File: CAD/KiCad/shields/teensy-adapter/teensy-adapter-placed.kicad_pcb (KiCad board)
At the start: 2 copper layers, 53.3 x 101.6 mm, 73 parts, among them U1 SN74LV4T125PWR, U2 SN74LV4T125PWR, U3 SN74LV4T125PWR, U4 SN74LV4T125PWR

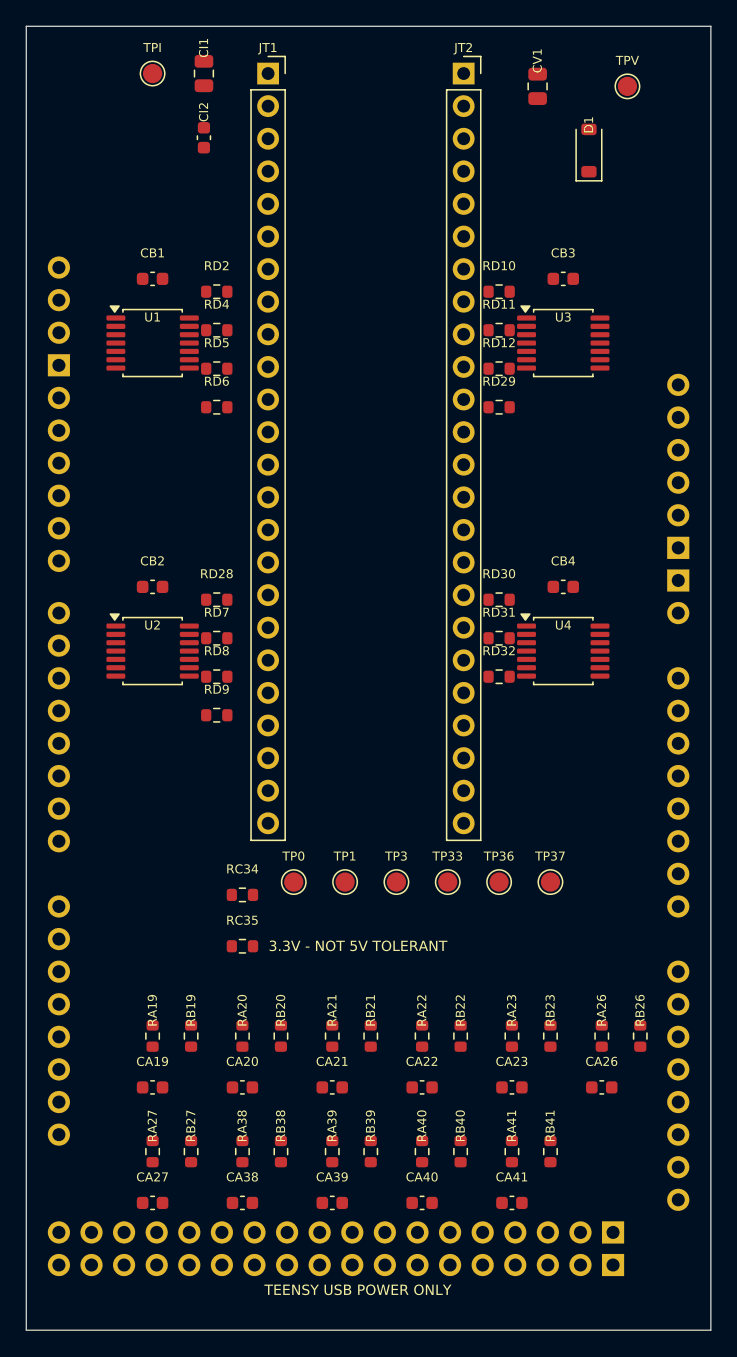
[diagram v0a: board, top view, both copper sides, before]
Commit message: Route the shield set and validate shared interfaces
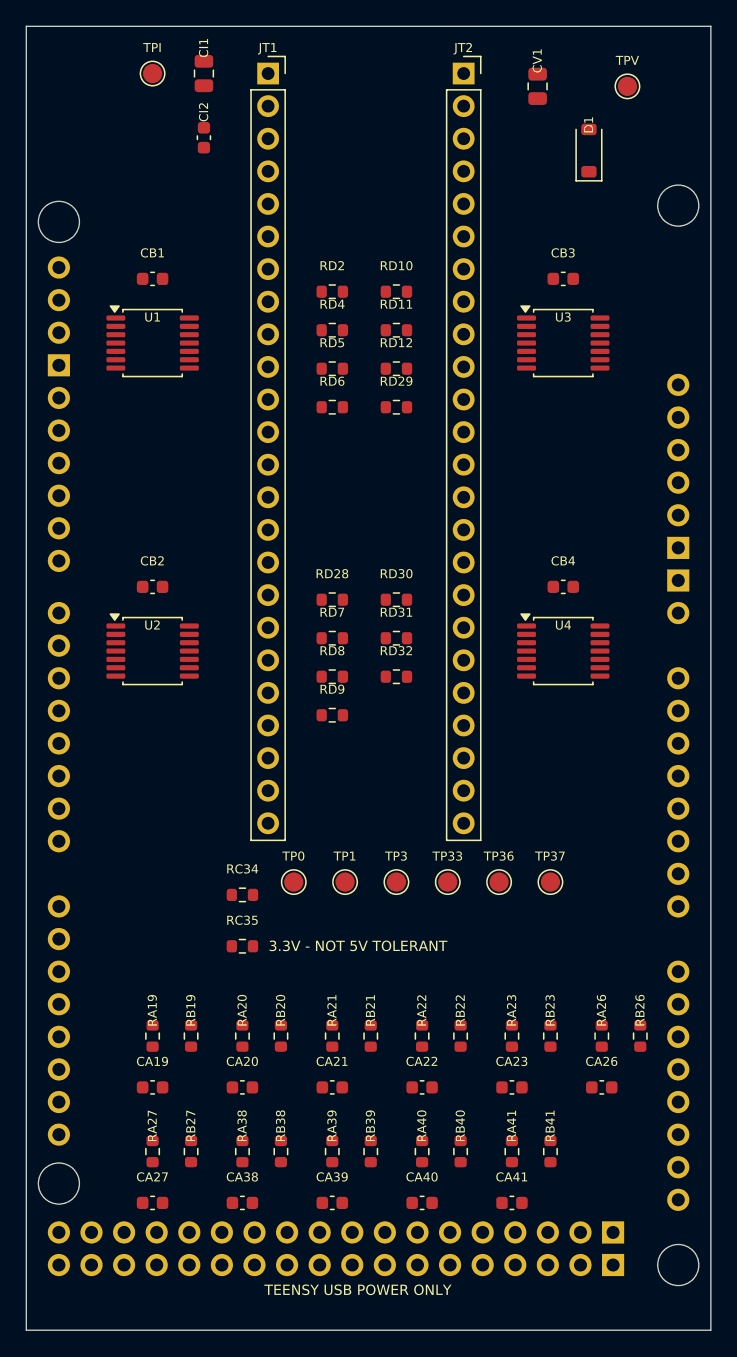
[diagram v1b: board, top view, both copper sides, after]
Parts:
- added HM1: M3 computing shield, Shields:MountingHole_3.2mm_M3, F.Cu at (192.0, 149.8)
- added HM2: M3 computing shield, Shields:MountingHole_3.2mm_M3, F.Cu at (143.7, 68.6)
- added HM3: M3 computing shield, Shields:MountingHole_3.2mm_M3, F.Cu at (143.7, 143.5)
- added HM4: M3 computing shield, Shields:MountingHole_3.2mm_M3, F.Cu at (192.0, 67.3)
- moved RD2 9.00 mm to (165.0, 74.0)
- moved RD28 9.00 mm to (165.0, 98.0)
- moved RD4 9.00 mm to (165.0, 77.0)
- moved RD5 9.00 mm to (165.0, 80.0)
- moved RD6 9.00 mm to (165.0, 83.0)
- moved RD7 9.00 mm to (165.0, 101.0)
- moved RD8 9.00 mm to (165.0, 104.0)
- moved RD9 9.00 mm to (165.0, 107.0)
- moved RD10 8.00 mm to (170.0, 74.0)
- moved RD11 8.00 mm to (170.0, 77.0)
- moved RD12 8.00 mm to (170.0, 80.0)
- moved RD29 8.00 mm to (170.0, 83.0)
- moved RD30 8.00 mm to (170.0, 98.0)
- moved RD31 8.00 mm to (170.0, 101.0)
- moved RD32 8.00 mm to (170.0, 104.0)

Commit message: Remove shield identification and adopt the simplified connector and Teensy pin maps
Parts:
- added TP40: gpio/40, Shields:TestPoint_Pad_D1.5mm, F.Cu at (186.0, 120.0)
- added TP41: gpio/41, Shields:TestPoint_Pad_D1.5mm, F.Cu at (190.0, 120.0)
- added TPG: GND, Shields:TestPoint_Pad_D1.5mm, F.Cu at (185.0, 124.0)
- D1: value SS14 -> 1N5819HW
- renumbered CA26 to CA24, CA27 to CA25, CA38 to CA26, CA39 to CA27, CA40 to CA38, CA41 to CA39, RA26 to RA24, RA27 to RA25, RA38 to RA26, RA39 to RA27, RA40 to RA38, RA41 to RA39, RB26 to RB24, RB27 to RB25, RB38 to RB26, RB39 to RB27, RB40 to RB38, RB41 to RB39
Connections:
- CA24 pad 1: adc/26 -> adc/24
- CA25 pad 1: adc/27 -> adc/25
- CA26 pad 1: adc/38 -> adc/26
- CA27 pad 1: adc/39 -> adc/27
- CA38 pad 1: adc/40 -> adc/38
- CA39 pad 1: adc/41 -> adc/39
- JM1 pad SCL: shield/scl -> (no net)
- JM1 pad SDA: shield/sda -> (no net)
- JT1 pad 16: shield/scl -> adc/24
- JT1 pad 17: shield/sda -> adc/25
- JT2 pad 16: adc/41 -> gpio/41
- JT2 pad 17: adc/40 -> gpio/40
- RA24 pad 2: adc/26 -> adc/24
- RA25 pad 2: adc/27 -> adc/25
- RA26 pad 2: adc/38 -> adc/26
- RA27 pad 2: adc/39 -> adc/27
- RA38 pad 2: adc/40 -> adc/38
- RA39 pad 2: adc/41 -> adc/39
- RB24 pad 1: adc/26 -> adc/24
- RB25 pad 1: adc/27 -> adc/25
- RB26 pad 1: adc/38 -> adc/26
- RB27 pad 1: adc/39 -> adc/27
- RB38 pad 1: adc/40 -> adc/38
- RB39 pad 1: adc/41 -> adc/39

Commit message: Route microphones directly to Teensy and remove the analyser buffer board
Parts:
- removed RC34, RC35: 100R, Shields:R_0603_1608Metric
- added CM1: 1nF C0G, Shields:C_0603_1608Metric, B.Cu at (178.4, 87.5)
- added CM2: 1nF C0G, Shields:C_0603_1608Metric, B.Cu at (178.4, 84.9)
- added CM3: 1nF C0G, Shields:C_0603_1608Metric, B.Cu at (178.4, 82.4)
- added CM4: 1nF C0G, Shields:C_0603_1608Metric, B.Cu at (178.4, 79.9)
- added CM5: 1nF C0G, Shields:C_0603_1608Metric, B.Cu at (178.4, 74.5)
- added TP34: gpio/34, Shields:TestPoint_Pad_D1.5mm, F.Cu at (157.2, 121.0)
- added TP35: gpio/35, Shields:TestPoint_Pad_D1.5mm, F.Cu at (157.2, 125.0)
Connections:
- JM1 pad A0: female1/analyser out -> (no net)
- JM1 pad A1: female2/analyser out -> (no net)
- JM1 pad A2: female3/analyser out -> (no net)
- JM1 pad A3: male1/analyser out -> (no net)
- JM1 pad A4: male2/analyser out -> (no net)
- JM1 pad D26: (no net) -> female1/mic direct
- JM1 pad D27: (no net) -> female2/mic direct
- JM1 pad D28: (no net) -> female3/mic direct
- JM1 pad D29: (no net) -> male1/mic direct
- JM1 pad D3: analyser/reset -> (no net)
- JM1 pad D30: (no net) -> male2/mic direct
- JM1 pad D4: analyser/strobe -> (no net)
- JM1 pad IORF: IOREF -> (no net)
- JT2 pad 10: male1/analyser out -> male1/mic direct
- JT2 pad 11: female3/analyser out -> female3/mic direct
- JT2 pad 12: female2/analyser out -> female2/mic direct
- JT2 pad 13: female1/analyser out -> female1/mic direct
- JT2 pad 9: male2/analyser out -> male2/mic direct
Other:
- copper layers 2 -> 4
- board text added: "0"
- board text added: "1"
- board text added: "3"
- board text added: "3.3 V NOT 5 V TOLERANT"
- board text added: "33"
- board text added: "34"
- board text added: "35"
- board text added: "36"
- board text added: "37"
- board text added: "3V3"
- board text added: "40"
- board text added: "41"
- board text added: "GND"
- board text added: "PIN 0"
- board text added: "POWERED BY TEENSY USB"
- board text added: "TEENSY 4.1 ADAPTER IN PLACE OF THE MEGA FIRMWARE 5"
- board text added: "USB ^"
- board text added: "VIN"
- board text removed: "3.3V - NOT 5V TOLERANT"
- board text removed: "TEENSY USB POWER ONLY"

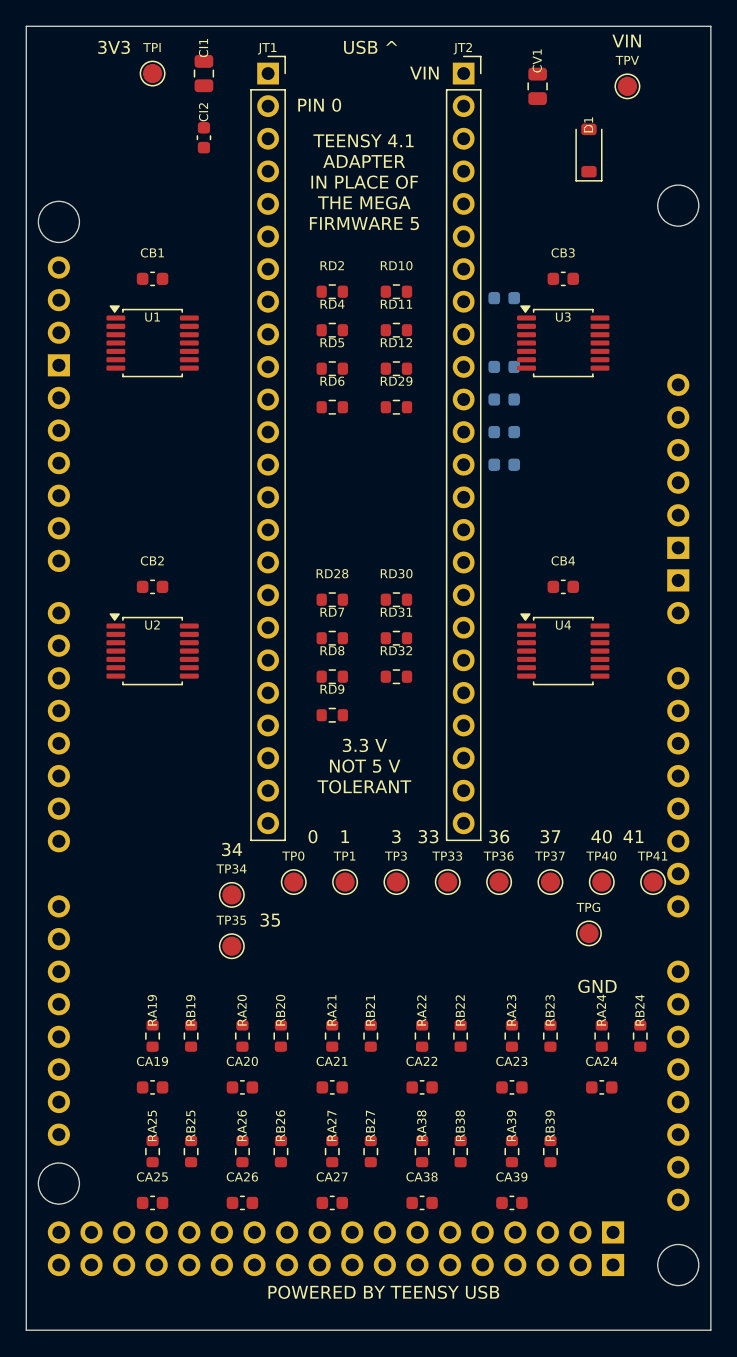
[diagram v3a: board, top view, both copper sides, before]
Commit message: Update shields for Thomas RC cards, debug headers and body microphones
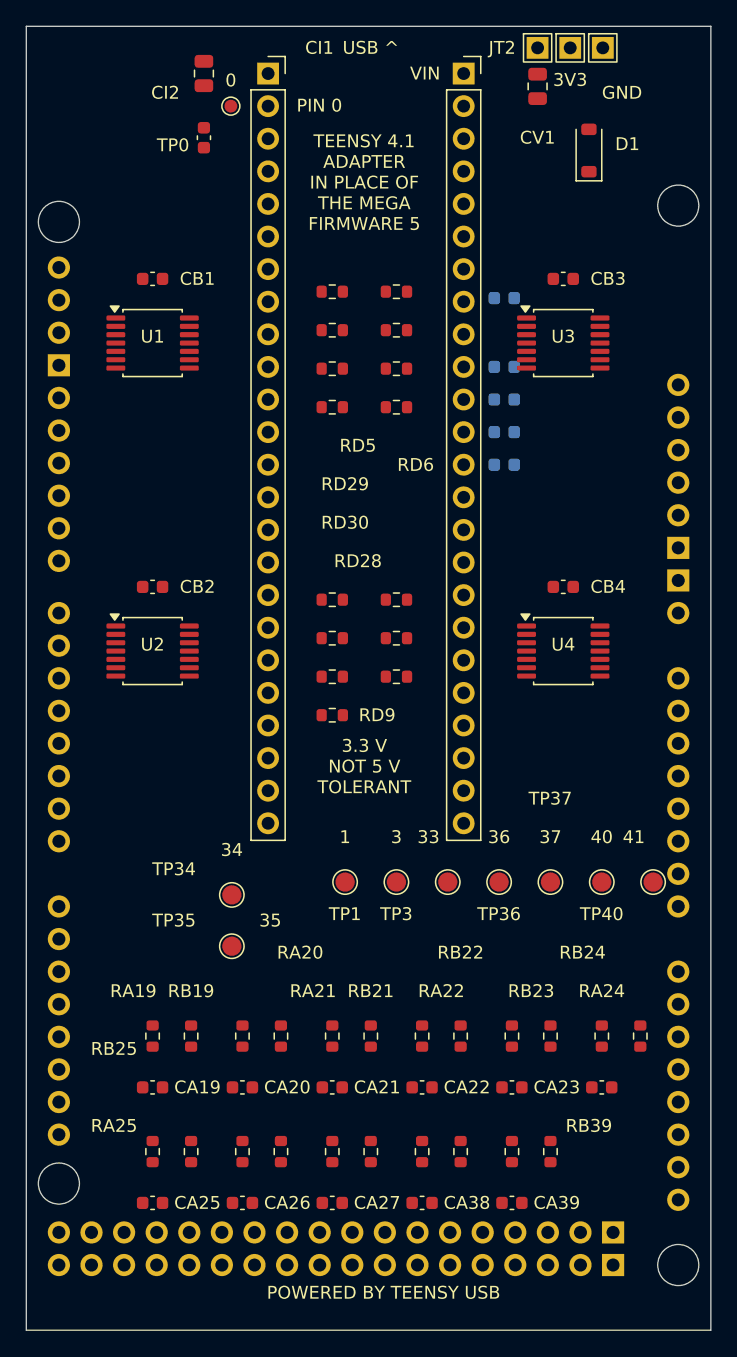
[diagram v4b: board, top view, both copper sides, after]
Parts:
- removed the TPG at (185.0, 124.0)
- removed the TPI at (151.0, 57.0)
- removed the TPV at (188.0, 58.0)
- added TPG: GND, Shields:TestPin_1x01_P2.54mm, F.Cu at (186.1, 55.0)
- added TPI: IOREF, Shields:TestPin_1x01_P2.54mm, F.Cu at (183.5, 55.0)
- added TPV: VIN_USB, Shields:TestPin_1x01_P2.54mm, F.Cu at (181.0, 55.0)
- TP0: footprint Shields:TestPoint_Pad_D1.5mm -> Shields:TestPoint_Pad_D1.0mm
- moved TP0 60.7 mm to (157.1, 59.5)

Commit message: Keep shield SMD on the front and supply voice cards for hand assembly
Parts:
- CM1, CM2, CM3, CM4, CM5: moved to F.Cu
- moved CM1 6.51 mm to (172.4, 90.0), turned to 90 degrees
- moved CM2 6.20 mm to (172.4, 86.5), turned to 90 degrees
- moved CM5 6.18 mm to (172.4, 76.0), turned to 90 degrees
- moved CM3 6.03 mm to (172.4, 83.0), turned to 90 degrees
- moved CM4 6.01 mm to (172.4, 79.5), turned to 90 degrees
